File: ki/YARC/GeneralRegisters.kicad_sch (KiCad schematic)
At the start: 13 parts, among them U71 74LS670, U72 74LS670, U73 74LS157, U74 74LS670, U75 74LS670, U76 74LS157, U77 74LS670, U78 74LS670, U79 74LS157, U80 74LS670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

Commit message: Ongoing schematic changes
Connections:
- net grclk renamed GECLK
- net ~{REG_WR} renamed ~{DST_EN_DLY}
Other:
- note added: "General Register Clocked Enable"
- note added: "Register Write Clock"
- note removed: "The Register Control Word (RCW) is made up of fields SRC1 (2 bits), SRC2 (3 bits), and DST(3 bits)."

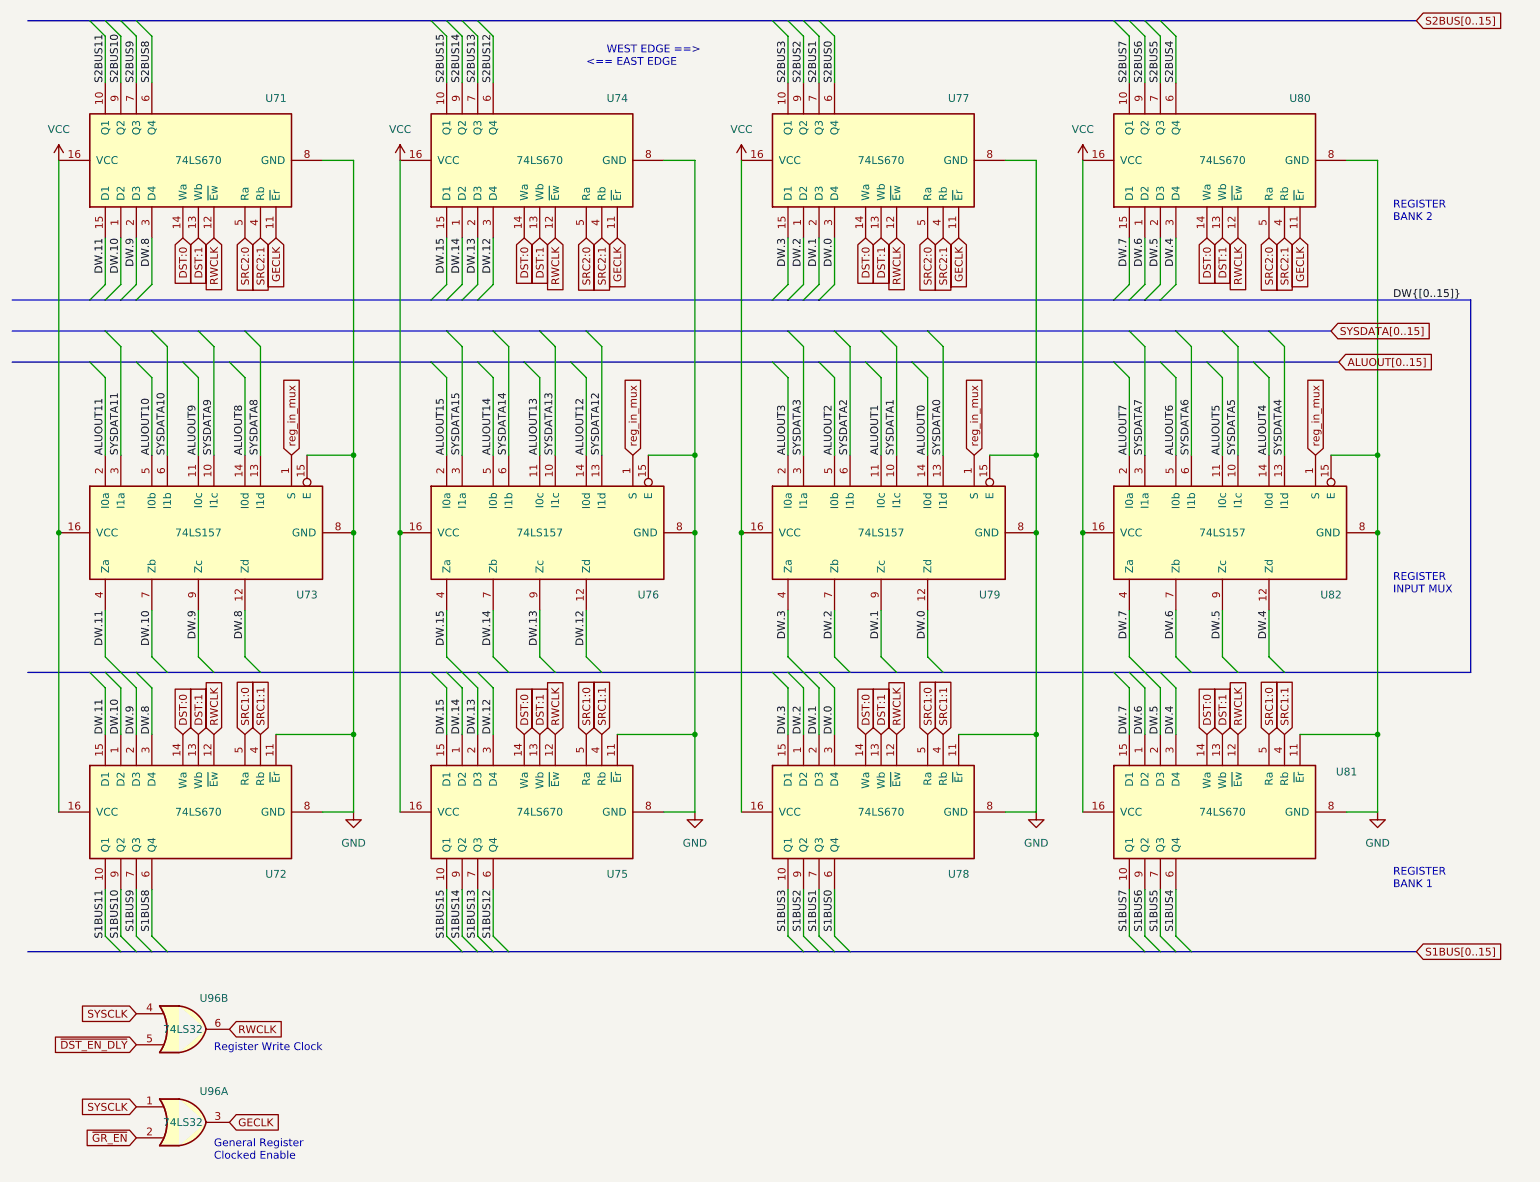
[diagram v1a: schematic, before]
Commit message: Schematic for addressing unit is complete and all ERC violations addressed
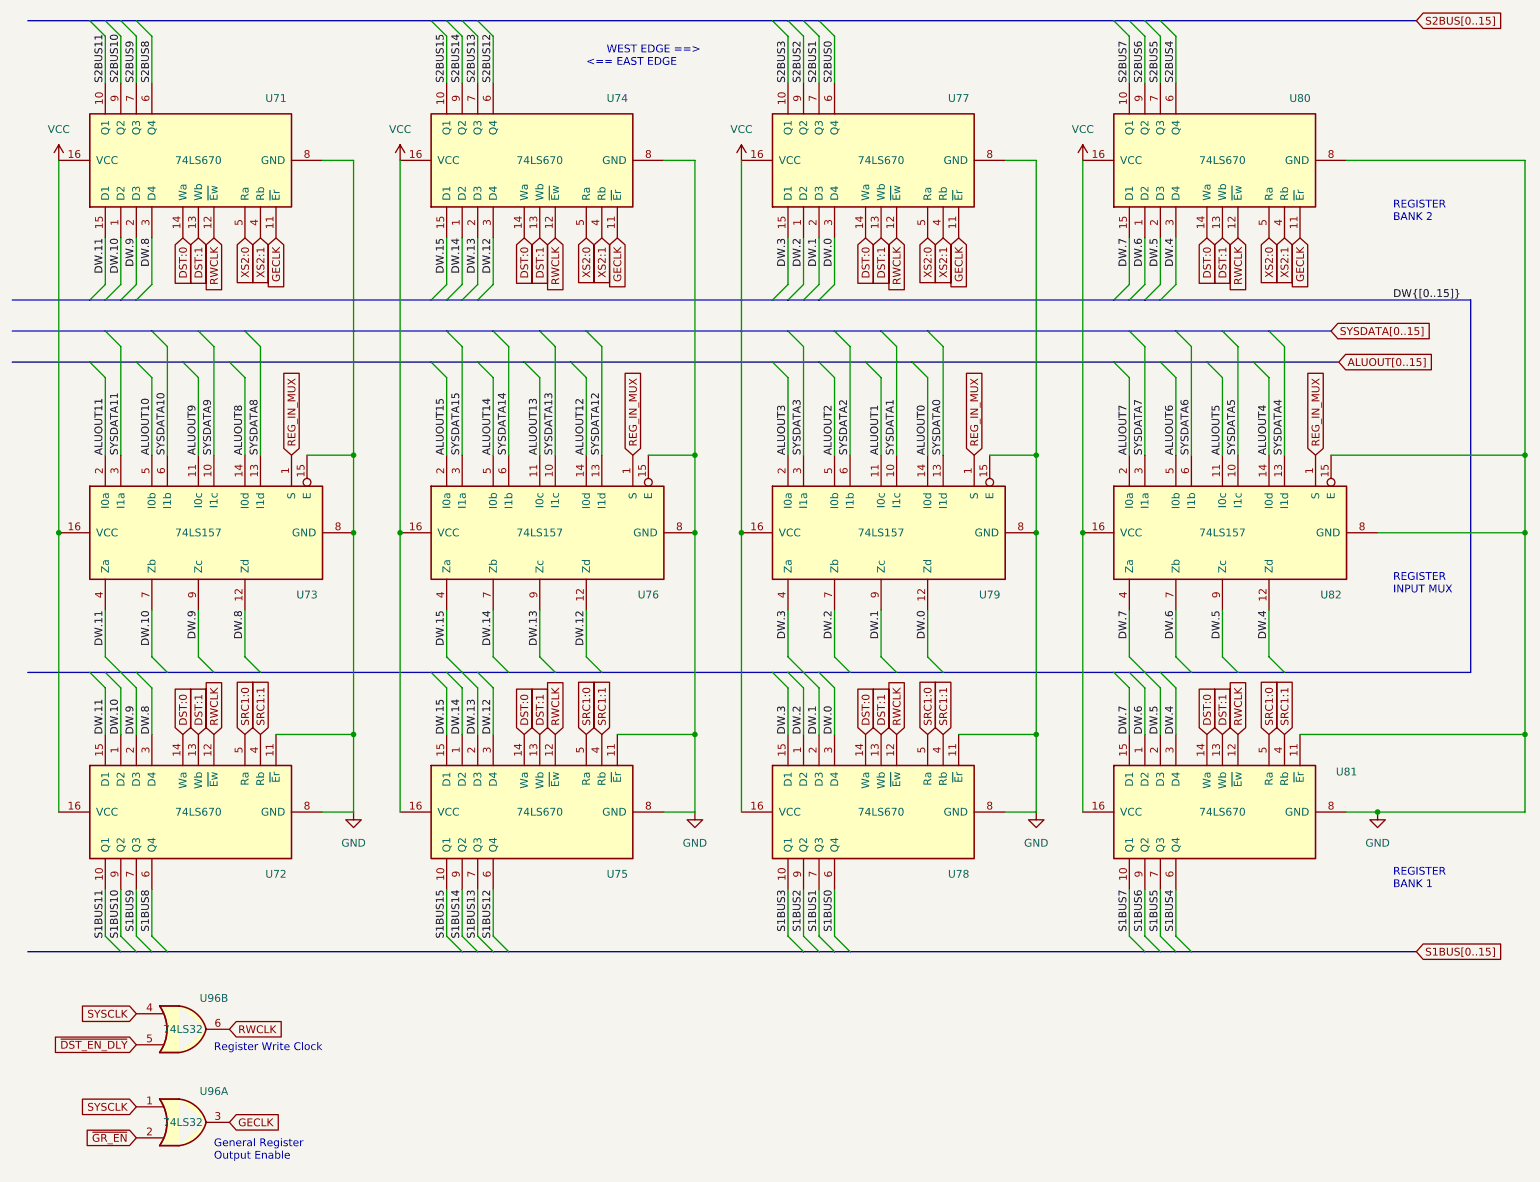
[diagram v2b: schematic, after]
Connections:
- net SRC2:0 renamed XS2:0
- net SRC2:1 renamed XS2:1
- net reg_in_mux renamed REG_IN_MUX
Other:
- note added: "General Register Output Enable"
- note removed: "General Register Clocked Enable"
